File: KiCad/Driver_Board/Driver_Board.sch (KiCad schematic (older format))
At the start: 0 parts

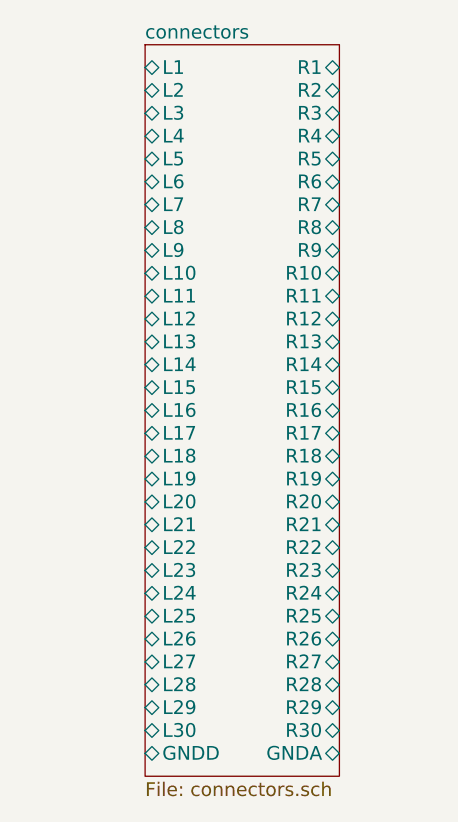
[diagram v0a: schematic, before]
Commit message: Updated connectors to reflect power board nets
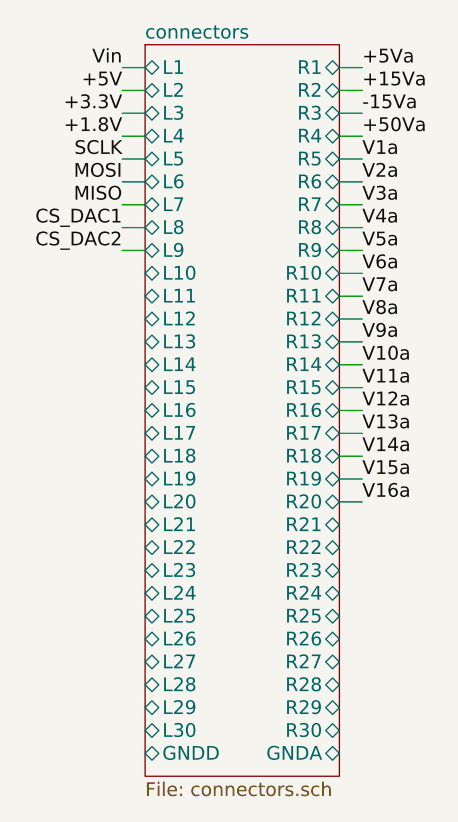
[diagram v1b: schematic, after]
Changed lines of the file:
@@
 F63 "GNDA" B R 2050 3750 60
 $EndSheet
+Wire Wire Line
+	1200 750  1100 750
+Wire Wire Line
+	1200 850  1100 850
+Wire Wire Line
+	1200 950  1100 950
+Wire Wire Line
+	1200 1050 1100 1050
+Wire Wire Line
+	1200 1150 1100 1150
+Wire Wire Line
+	1200 1250 1100 1250
+Wire Wire Line
+	1200 1350 1100 1350
+Wire Wire Line
+	1200 1450 1100 1450
+Wire Wire Line
+	1200 1550 1100 1550
+Wire Wire Line
+	2050 750  2150 750
+Wire Wire Line
+	2050 850  2150 850
+Wire Wire Line
+	2050 950  2150 950
+Wire Wire Line
+	2050 1050 2150 1050
+Wire Wire Line
+	2050 1150 2150 1150
+Wire Wire Line
+	2050 1250 2150 1250
+Wire Wire Line
+	2050 2650 2150 2650
+Wire Wire Line
+	2050 2550 2150 2550
+Wire Wire Line
+	2050 2450 2150 2450
+Wire Wire Line
+	2050 2350 2150 2350
+Wire Wire Line
+	2050 2250 2150 2250
+Wire Wire Line
+	2050 2150 2150 2150
+Wire Wire Line
+	2050 2050 2150 2050
+Wire Wire Line
+	2050 1950 2150 1950
+Wire Wire Line
+	2050 1850 2150 1850
+Wire Wire Line
+	2050 1750 2150 1750
+Wire Wire Line
+	2050 1650 2150 1650
+Wire Wire Line
+	2050 1550 2150 1550
+Wire Wire Line
+	2050 1450 2150 1450
+Wire Wire Line
+	2050 1350 2150 1350
+Text Label 1100 750  2    60   ~ 0
+Vin
+Text Label 1100 850  2    60   ~ 0
++5V
+Text Label 1100 950  2    60   ~ 0
++3.3V
+Text Label 1100 1050 2    60   ~ 0
++1.8V
+Text Label 1100 1150 2    60   ~ 0
+SCLK
+Text Label 1100 1250 2    60   ~ 0
+MOSI
+Text Label 1100 1350 2    60   ~ 0
+MISO
+Text Label 1100 1450 2    60   ~ 0
+CS_DAC1
+Text Label 1100 1550 2    60   ~ 0
+CS_DAC2
+Text Label 2150 750  0    60   ~ 0
++5Va
+Text Label 2150 850  0    60   ~ 0
++15Va
+Text Label 2150 950  0    60   ~ 0
+-15Va
+Text Label 2150 1050 0    60   ~ 0
++50Va
+Text Label 2150 1150 0    60   ~ 0
+V1a
+Text Label 2150 1250 0    60   ~ 0
+V2a
+Text Label 2150 1350 0    60   ~ 0
+V3a
+Text Label 2150 1450 0    60   ~ 0
+V4a
+Text Label 2150 1550 0    60   ~ 0
+V5a
+Text Label 2150 1650 0    60   ~ 0
+V6a
+Text Label 2150 1750 0    60   ~ 0
+V7a
+Text Label 2150 1850 0    60   ~ 0
+V8a
+Text Label 2150 1950 0    60   ~ 0
+V9a
+Text Label 2150 2050 0    60   ~ 0
+V10a
+Text Label 2150 2150 0    60   ~ 0
+V11a
+Text Label 2150 2250 0    60   ~ 0
+V12a
+Text Label 2150 2350 0    60   ~ 0
+V13a
+Text Label 2150 2450 0    60   ~ 0
+V14a
+Text Label 2150 2550 0    60   ~ 0
+V15a
+Text Label 2150 2650 0    60   ~ 0
+V16a
 $EndSCHEMATC
